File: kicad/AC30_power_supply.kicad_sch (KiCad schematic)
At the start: 15 parts, among them IC16 7805, P1 120 VAC line cord, T1 120/240V : 18VAC CT 300mA

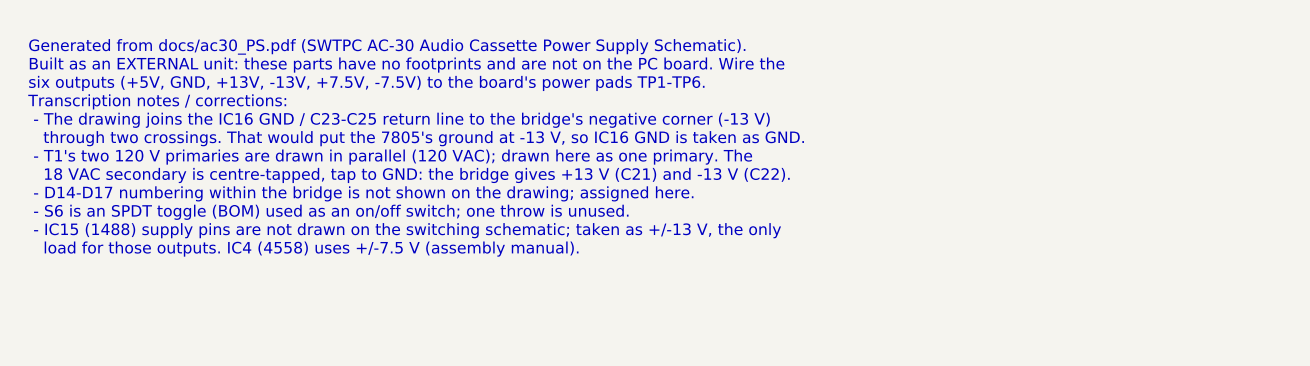
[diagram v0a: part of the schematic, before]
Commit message: Replace power input pads with J12, a 6-pin KK-396 header on the bottom edge
- J12 (Molex KK-396 A-41791-0006) replaces solder pads TP1-TP6 for the
  external supply: 1 GND, 2 +5V, 3 +13V, 4 -13V, 5 +7.5V, 6 -7.5V.
  Placed in the bottom connector row next to J2, clear of the corner hole.
- build.sh: if no routing attempt is DRC-clean, up to 3 finishing passes
  route only what is left on the best result, each checked by DRC.
- Board 173.5 x 122.0 mm, fully routed; ERC, DRC (all severities) and
  schematic parity clean. AC30-settings.md updated (power input, drill
  table, routing, positions).

Co-Authored-By: Claude Opus 5.5 <noreply@anthropic.com>
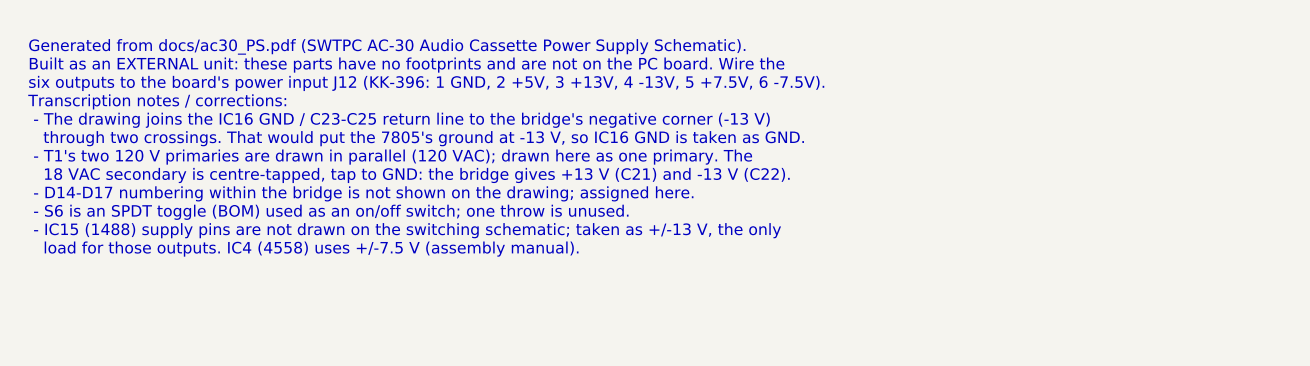
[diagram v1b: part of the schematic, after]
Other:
- note added: "Generated from docs/ac30_PS.pdf (SWTPC AC-30 Audio Cassette Power Supply Schematic). Built as an EXTERNAL unit: these parts have no footprints and are not on the PC board. Wire the six outputs to the board's power input J12 (KK-396: 1 GND, 2 +5V, 3 +13V, 4 -13V, 5 +7.5V, 6 -7.5V). Transcription notes / corrections: - The drawing joins the IC16 GND / C23-C25 return line to the bridge's negative co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"
- note removed: "Generated from docs/ac30_PS.pdf (SWTPC AC-30 Audio Cassette Power Supply Schematic). Built as an EXTERNAL unit: these parts have no footprints and are not on the PC board. Wire the six outputs (+5V, GND, +13V, -13V, +7.5V, -7.5V) to the board's power pads TP1-TP6. Transcription notes / corrections: - The drawing joins the IC16 GND / C23-C25 return line to the bridge's negative corner (-13 V) thro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"
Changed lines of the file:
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@@
 		(comment 1 "Source: docs/ac30_PS.pdf; parts have no footprints - built as a separate unit")
 	)
-	(text "Generated from docs/ac30_PS.pdf (SWTPC AC-30 Audio Cassette Power Supply Schematic).\nBuilt as an EXTERNAL unit: these parts have no footprints and are not on the PC board. Wire the\nsix outputs (+5V, GND, +13V, -13V, +7.5V, -7.5V) to the board's power pads TP1-TP6.\nTranscription notes / corrections:\n - The drawing joins the IC16 GND / C23-C25 return line to the bridge's negative corner (-13 V)\n   through two crossings. That would put the 7805's ground at -13 V, so IC16 GND is taken as GND.\n - T1's two 120 V primaries are drawn in parallel (120 VAC); drawn here as one primary. The\n   18 VAC secondary is centre-tapped, tap to GND: the bridge gives +13 V (C21) and -13 V (C22).\n - D14-D17 numbering within the bridge is not shown on the drawing; assigned here.\n - S6 is an SPDT toggle (BOM) used as an on/off switch; one throw is unused.\n - IC15 (1488) supply pins are not drawn on the switching schematic; taken as +/-13 V, the only\n   load for those outputs. IC4 (4558) uses +/-7.5 V (assembly manual)."
+	(text "Generated from docs/ac30_PS.pdf (SWTPC AC-30 Audio Cassette Power Supply Schematic).\nBuilt as an EXTERNAL unit: these parts have no footprints and are not on the PC board. Wire the\nsix outputs to the board's power input J12 (KK-396: 1 GND, 2 +5V, 3 +13V, 4 -13V, 5 +7.5V, 6 -7.5V).\nTranscription notes / corrections:\n - The drawing joins the IC16 GND / C23-C25 return line to the bridge's negative corner (-13 V)\n   through two crossings. That would put the 7805's ground at -13 V, so IC16 GND is taken as GND.\n - T1's two 120 V primaries are drawn in parallel (120 VAC); drawn here as one primary. The\n   18 VAC secondary is centre-tapped, tap to GND: the bridge gives +13 V (C21) and -13 V (C22).\n - D14-D17 numbering within the bridge is not shown on the drawing; assigned here.\n - S6 is an SPDT toggle (BOM) used as an on/off switch; one throw is unused.\n - IC15 (1488) supply pins are not drawn on the switching schematic; taken as +/-13 V, the only\n   load for those outputs. IC4 (4558) uses +/-7.5 V (assembly manual)."
 		(exclude_from_sim no)
 		(at 20.32 15.24 0)

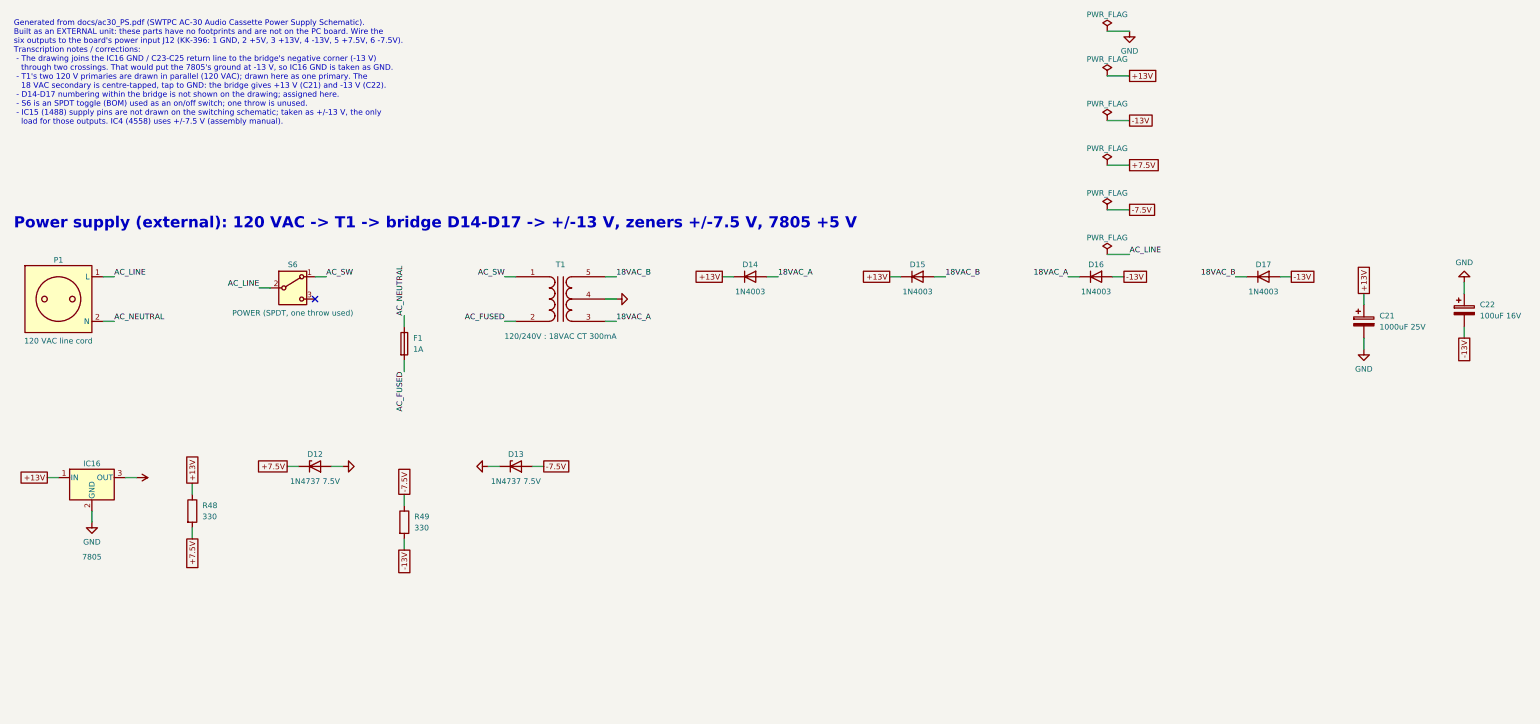
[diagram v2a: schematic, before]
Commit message: Wired, human-readable schematics with PDF and PNG images
gen.py now lays out each functional group on its own and draws its nets
as real wires (new tools/schroute.py: orthogonal grid router that never
ends, bends or overlaps on another net's wire); every routed net keeps
one label with its name, labels join nets between blocks and sheets, and
unroutable connections fall back to label pairs (17). The front-panel
jumper pads share the front-panel block. Custom 1488/1489 output pins
moved onto the 2.54 mm grid.

build.sh exports schematic/<project>.pdf and, via tools/schimg.py, PNGs
of every sheet and functional block for both boards.

Connectivity unchanged (pin-to-net maps identical for both variants);
ERC 0; both PCBs DRC/parity clean and unchanged. Docs updated.

Co-Authored-By: Claude Opus 5.5 <noreply@anthropic.com>
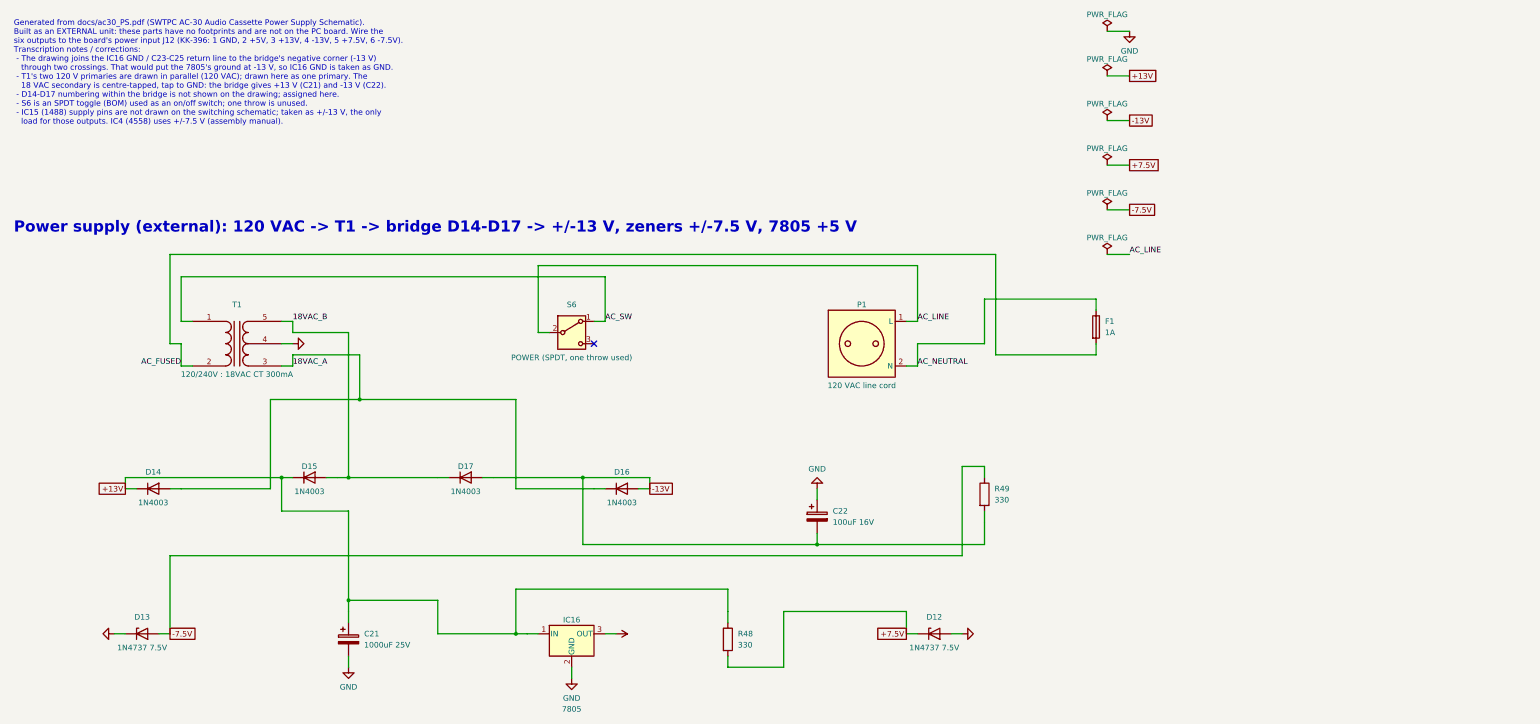
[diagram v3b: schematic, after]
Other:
- moved on the sheet: C21, C22, D12, D13, D14, D15, D16, D17, F1, IC16, P1, R48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
